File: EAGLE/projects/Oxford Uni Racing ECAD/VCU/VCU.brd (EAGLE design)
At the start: 165.1 x 114 mm, 15 parts, among them J1 PWR_CAN, J3 MC_LEFT, J4 MC_RIGHT, X2 D-SUB9-H2M09ST

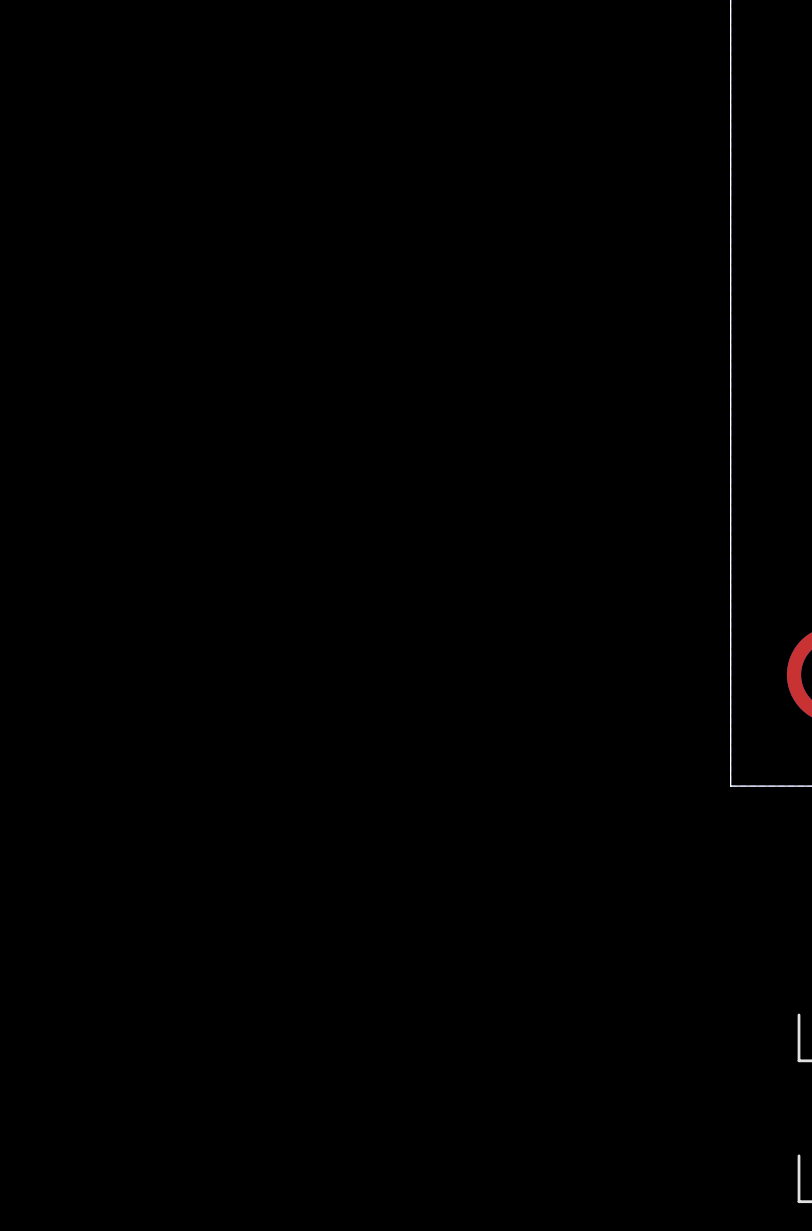
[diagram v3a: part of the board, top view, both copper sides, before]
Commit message: added microcontroller to VCU and wired Motor Controllers
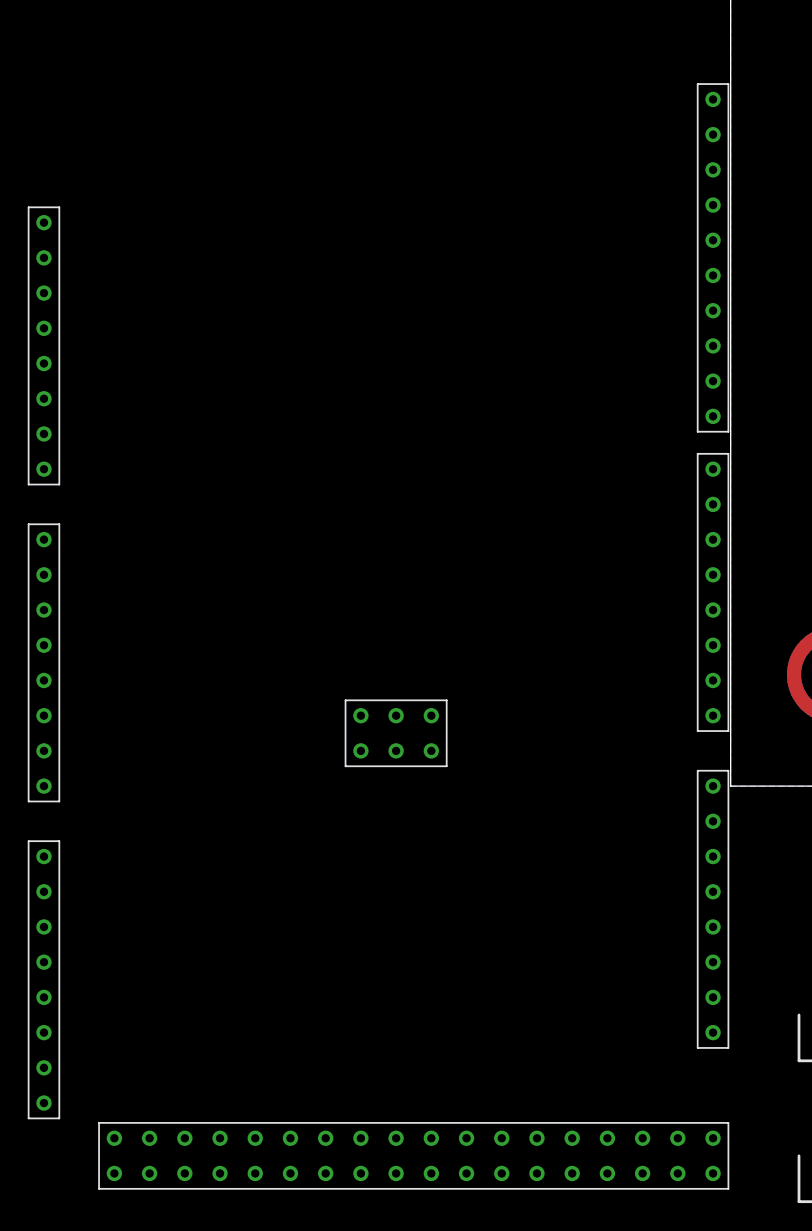
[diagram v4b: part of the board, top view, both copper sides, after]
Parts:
- added U$1: SAME70-XPLD, Oxford Uni Racing Custom Blueprints:SAME70-XPLD
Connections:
- removed net MC_1_BRAKE_INPUT: J3.1
- removed net MC_1_IMPULSE_INPUT: J3.4
- removed net MC_1_REVERSE_SWITCH: J3.7
- removed net MC_2_BRAKE_INPUT: J4.1
- removed net MC_2_IMPULSE_INPUT: J4.4
- removed net MC_2_REVERSE_SWITCH: J4.7
- net GND: now also J3.1, J3.4, J3.7, J4.1, J4.4, J4.7
- net MC_1_RXD: now also U$1.J5034
- net MC_1_THROTTLE_INPUT: now also U$1.J5044
- net MC_1_TXD: now also U$1.J5035
- net MC_2_RXD: now also U$1.J5020
- net MC_2_THROTTLE_INPUT: now also U$1.J5045
- net MC_2_TXD: now also U$1.J5007
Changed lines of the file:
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@@
 <attribute name="VALUE" x="10.16" y="-26.67" size="1.27" layer="27" align="center"/>
 </element>
+<element name="U$1" library="Oxford Uni Racing Custom Blueprints" package="SAME70-XPLD" value="SAME70-XPLD" x="-49.53" y="-22.86" smashed="yes"/>
 </elements>
 <signals>
@@
 <contactref element="J3" pad="8"/>
 <contactref element="J4" pad="8"/>
+<contactref element="J3" pad="7"/>
+<contactref element="J3" pad="1"/>
+<contactref element="J3" pad="4"/>
+<contactref element="J4" pad="1"/>
+<contactref element="J4" pad="7"/>
+<contactref element="J4" pad="4"/>
 <wire x1="119.38" y1="17.78" x2="130.81" y2="10.16" width="0" layer="19" extent="16-16"/>
 <wire x1="100.33" y1="11.43" x2="110.49" y2="10.16" width="0" layer="19" extent="16-16"/>
 <wire x1="17.78" y1="-13.97" x2="91.44" y2="8.7376" width="0" layer="19" extent="1-1"/>
-<wire x1="17.78" y1="-24.13" x2="17.78" y2="-13.97" width="0" layer="19" extent="1-1"/>
+<wire x1="17.78" y1="-16.51" x2="17.78" y2="-13.97" width="0" layer="19" extent="1-1"/>
+<wire x1="12.7" y1="-13.97" x2="17.78" y2="-13.97" width="0" layer="19" extent="1-1"/>
+<wire x1="10.16" y1="-16.51" x2="12.7" y2="-13.97" width="0" layer="19" extent="1-1"/>
+<wire x1="17.78" y1="-24.13" x2="17.78" y2="-16.51" width="0" layer="19" extent="1-1"/>
+<wire x1="17.78" y1="-26.67" x2="17.78" y2="-24.13" width="0" layer="19" extent="1-1"/>
+<wire x1="12.7" y1="-24.13" x2="17.78" y2="-24.13" width="0" layer="19" extent="1-1"/>
+<wire x1="10.16" y1="-26.67" x2="12.7" y2="-24.13" width="0" layer="19" extent="1-1"/>
 </signal>
 <signal name="CANL">
@@
 <wire x1="144.78" y1="13.97" x2="144.78" y2="11.43" width="1.27" layer="16"/>
 </signal>
-<signal name="MC_1_BRAKE_INPUT">
-<contactref element="J3" pad="1"/>
-</signal>
-<signal name="MC_1_REVERSE_SWITCH">
-<contactref element="J3" pad="7"/>
-</signal>
-<signal name="MC_1_IMPULSE_INPUT">
-<contactref element="J3" pad="4"/>
-</signal>
 <signal name="MC_1_THROTTLE_INPUT">
 <contactref element="J3" pad="6"/>
+<contactref element="U$1" pad="J5044"/>
+<wire x1="15.24" y1="-13.97" x2="-49.53" y2="-15.24" width="0" layer="19" extent="1-1"/>
 </signal>
 <signal name="MC_1_RXD">
 <contactref element="J3" pad="3"/>
+<contactref element="U$1" pad="J5034"/>
+<wire x1="12.7" y1="-16.51" x2="-1.27" y2="12.7" width="0" layer="19" extent="1-1"/>
 </signal>
 <signal name="MC_1_TXD">
 <contactref element="J3" pad="5"/>
-</signal>
-<signal name="MC_2_BRAKE_INPUT">
-<contactref element="J4" pad="1"/>
+<contactref element="U$1" pad="J5035"/>
+<wire x1="15.24" y1="-16.51" x2="-1.27" y2="10.16" width="0" layer="19" extent="1-1"/>
 </signal>
 <signal name="MC_2_RXD">
 <contactref element="J4" pad="3"/>
+<contactref element="U$1" pad="J5020"/>
+<wire x1="12.7" y1="-26.67" x2="-49.53" y2="17.78" width="0" layer="19" extent="1-1"/>
 </signal>
 <signal name="MC_2_TXD">
 <contactref element="J4" pad="5"/>
-</signal>
-<signal name="MC_2_REVERSE_SWITCH">
-<contactref element="J4" pad="7"/>
-</signal>
-<signal name="MC_2_IMPULSE_INPUT">
-<contactref element="J4" pad="4"/>
+<contactref element="U$1" pad="J5007"/>
+<wire x1="15.24" y1="-26.67" x2="-1.27" y2="31.75" width="0" layer="19" extent="1-1"/>
 </signal>
 <signal name="MC_2_THROTTLE_INPUT">
 <contactref element="J4" pad="6"/>
+<contactref element="U$1" pad="J5045"/>
+<wire x1="15.24" y1="-24.13" x2="-49.53" y2="-17.78" width="0" layer="19" extent="1-1"/>
 </signal>
 </signals>

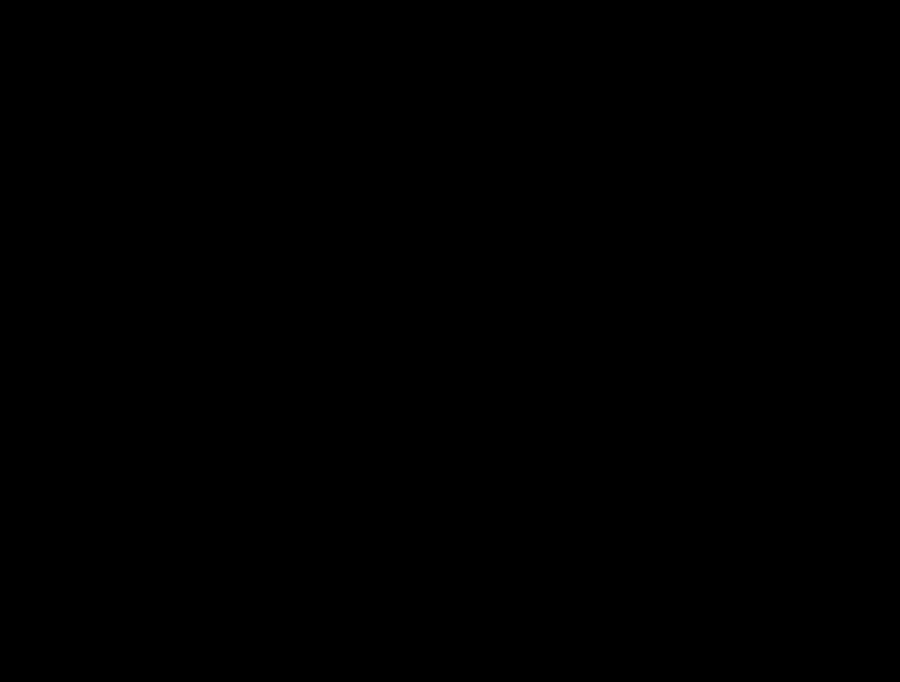
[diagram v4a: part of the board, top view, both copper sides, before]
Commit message: added CAN transciever to VCU
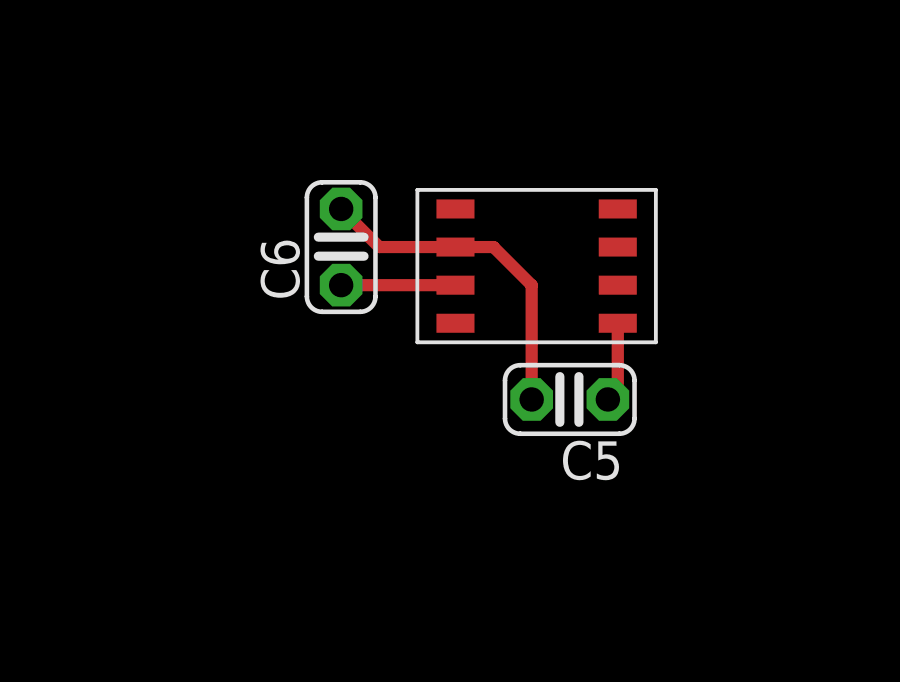
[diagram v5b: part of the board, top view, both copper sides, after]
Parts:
- added C5, C6: (no value), adafruit:C025-024X044
- added U$3: TCAN1042, TCAN1042:TCAN1042
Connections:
- new net CAN_STANDBY: U$1.J5032, U$3.PIN_7
- new net RXD: U$1.J5037, U$3.PIN_3
- new net TXD: U$1.J5036, U$3.PIN_0
- net 3.3V: now also C5.1, U$3.PIN_4
- net 5V: now also C6.1, U$3.PIN_2
- net CANH: now also U$3.PIN_6
- net CANL: now also U$3.PIN_5
- net GND: now also C5.2, C6.2, U$3.PIN_1
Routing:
- net GND: track 72.8 -> 84.0 mm
- net 5V: track 17.8 -> 21.6 mm
- net 3.3V: track 17.8 -> 20.5 mm
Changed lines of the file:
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@@
 </element>
 <element name="U$1" library="Oxford Uni Racing Custom Blueprints" package="SAME70-XPLD" value="SAME70-XPLD" x="-49.53" y="-22.86" smashed="yes"/>
+<element name="U$3" library="TCAN1042" package="TCAN1042" value="TCAN1042" x="86.36" y="63.5" smashed="yes"/>
+<element name="C5" library="adafruit" library_urn="urn:adsk.eagle:library:420" package="C025-024X044" package3d_urn="urn:adsk.eagle:package:6240324/1" value="" x="96.52" y="59.69" smashed="yes" rot="R180">
+<attribute name="NAME" x="98.298" y="58.293" size="1.27" layer="25" ratio="10" rot="R180"/>
+<attribute name="VALUE" x="98.298" y="62.357" size="1.27" layer="27" ratio="10" rot="R180"/>
+</element>
+<element name="C6" library="adafruit" library_urn="urn:adsk.eagle:library:420" package="C025-024X044" package3d_urn="urn:adsk.eagle:package:6240324/1" value="" x="88.9" y="64.77" smashed="yes" rot="R90">
+<attribute name="NAME" x="87.503" y="62.992" size="1.27" layer="25" ratio="10" rot="R90"/>
+<attribute name="VALUE" x="91.567" y="62.992" size="1.27" layer="27" ratio="10" rot="R90"/>
+</element>
 </elements>
 <signals>
@@
 <contactref element="J4" pad="7"/>
 <contactref element="J4" pad="4"/>
-<wire x1="119.38" y1="17.78" x2="130.81" y2="10.16" width="0" layer="19" extent="16-16"/>
-<wire x1="100.33" y1="11.43" x2="110.49" y2="10.16" width="0" layer="19" extent="16-16"/>
+<contactref element="C6" pad="2"/>
+<contactref element="U$3" pad="PIN_1"/>
+<contactref element="C5" pad="2"/>
+<wire x1="92.71" y1="64.77" x2="90.17" y2="64.77" width="0.4064" layer="1"/>
+<wire x1="90.17" y1="64.77" x2="88.9" y2="66.04" width="0.4064" layer="1"/>
+<wire x1="92.71" y1="64.77" x2="93.98" y2="64.77" width="0.4064" layer="1"/>
+<wire x1="93.98" y1="64.77" x2="95.25" y2="63.5" width="0.4064" layer="1"/>
+<wire x1="95.25" y1="63.5" x2="95.25" y2="59.69" width="0.4064" layer="1"/>
+<wire x1="96.52" y1="22.86" x2="95.25" y2="59.69" width="0" layer="19" extent="1-1"/>
+<wire x1="110.49" y1="10.16" x2="100.33" y2="11.43" width="0" layer="19" extent="16-16"/>
+<wire x1="130.81" y1="10.16" x2="119.38" y2="17.78" width="0" layer="19" extent="16-16"/>
 <wire x1="17.78" y1="-13.97" x2="91.44" y2="8.7376" width="0" layer="19" extent="1-1"/>
 <wire x1="17.78" y1="-16.51" x2="17.78" y2="-13.97" width="0" layer="19" extent="1-1"/>
@@
 <wire x1="94.2086" y1="8.7376" x2="94.10065" y2="8.84555" width="0.6096" layer="16"/>
 <wire x1="94.10065" y1="8.84555" x2="94.10065" y2="13.97" width="0.6096" layer="16"/>
+<contactref element="U$3" pad="PIN_5"/>
+<wire x1="93.98" y1="29.21" x2="98.1202" y2="63.5" width="0" layer="19" extent="1-1"/>
 <wire x1="93.98" y1="20.32" x2="93.98" y2="22.86" width="0" layer="19" extent="1-1"/>
 </signal>
@@
 <wire x1="91.44" y1="22.86" x2="86.36" y2="27.94" width="1.27" layer="16"/>
 <wire x1="86.36" y1="27.94" x2="86.36" y2="29.21" width="1.27" layer="16"/>
+<contactref element="U$3" pad="PIN_6"/>
+<wire x1="86.36" y1="29.21" x2="98.1202" y2="64.77" width="0" layer="19" extent="1-1"/>
 </signal>
 <signal name="5V">
@@
 <contactref element="J3" pad="2"/>
 <contactref element="J4" pad="2"/>
-<wire x1="87.2871" y1="11.5824" x2="142.24" y2="15.24" width="0" layer="19" extent="1-1"/>
+<contactref element="U$3" pad="PIN_2"/>
+<contactref element="C6" pad="1"/>
+<wire x1="92.71" y1="63.5" x2="88.9" y2="63.5" width="0.4064" layer="1"/>
+<wire x1="87.2871" y1="11.5824" x2="88.9" y2="63.5" width="0" layer="19" extent="1-1"/>
+<wire x1="142.24" y1="15.24" x2="87.2871" y2="11.5824" width="0" layer="19" extent="1-1"/>
 <wire x1="10.16" y1="-13.97" x2="87.2871" y2="11.5824" width="0" layer="19" extent="1-1"/>
 <wire x1="10.16" y1="-24.13" x2="10.16" y2="-13.97" width="0" layer="19" extent="1-1"/>
@@
 <wire x1="121.92" y1="21.59" x2="121.92" y2="22.86" width="1.27" layer="16"/>
 <wire x1="124.46" y1="21.59" x2="121.92" y2="21.59" width="1.27" layer="16"/>
+<contactref element="U$3" pad="PIN_4"/>
+<contactref element="C5" pad="1"/>
+<wire x1="98.1202" y1="62.23" x2="98.1202" y2="60.0202" width="0.4064" layer="1"/>
+<wire x1="98.1202" y1="60.0202" x2="97.79" y2="59.69" width="0.4064" layer="1"/>
+<wire x1="121.92" y1="22.86" x2="97.79" y2="59.69" width="0" layer="19" extent="16-16"/>
 </signal>
 <signal name="N$4">
@@
 <wire x1="15.24" y1="-24.13" x2="-49.53" y2="-17.78" width="0" layer="19" extent="1-1"/>
 </signal>
+<signal name="CAN_STANDBY">
+<contactref element="U$3" pad="PIN_7"/>
+<contactref element="U$1" pad="J5032"/>
+<wire x1="-1.27" y1="17.78" x2="98.1202" y2="66.04" width="0" layer="19" extent="1-1"/>
+</signal>
+<signal name="TXD">
+<contactref element="U$3" pad="PIN_0"/>
+<contactref element="U$1" pad="J5036"/>
+<wire x1="-1.27" y1="7.62" x2="92.71" y2="66.04" width="0" layer="19" extent="1-1"/>
+</signal>
+<signal name="RXD">
+<contactref element="U$3" pad="PIN_3"/>
+<contactref element="U$1" pad="J5037"/>
+<wire x1="-1.27" y1="5.08" x2="92.71" y2="62.23" width="0" layer="19" extent="1-1"/>
+</signal>
 </signals>
